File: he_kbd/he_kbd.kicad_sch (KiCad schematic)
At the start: 47 parts, among them U1 CD74HC4067M, U2 CD74HC4067M, U3 CD74HC4067M

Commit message: continue
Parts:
- U1, U2, U3: footprint Package_SO:TSSOP-24_4.4x7.8mm_P0.65mm -> Package_SO:SSOP-24_3.9x8.7mm_P0.635mm
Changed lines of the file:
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@@
 			)
 		)
-		(property "Footprint" "Package_SO:TSSOP-24_4.4x7.8mm_P0.65mm"
+		(property "Footprint" "Package_SO:SSOP-24_3.9x8.7mm_P0.635mm"
 			(at 130.81 59.69 0)
 			(effects
@@
 	)
 	(symbol
+		(lib_name "CD74HC4067M_1")
 		(lib_id "74xx:CD74HC4067M")
 		(at 63.5 120.65 270)
@@
 			)
 		)
-		(property "Footprint" "Package_SO:TSSOP-24_4.4x7.8mm_P0.65mm"
+		(property "Footprint" "Package_SO:SSOP-24_3.9x8.7mm_P0.635mm"
 			(at 38.1 143.51 0)
 			(effects
@@
 			)
 		)
-		(property "Footprint" "Package_SO:TSSOP-24_4.4x7.8mm_P0.65mm"
+		(property "Footprint" "Package_SO:SSOP-24_3.9x8.7mm_P0.635mm"
 			(at 215.9 59.69 0)
 			(effects

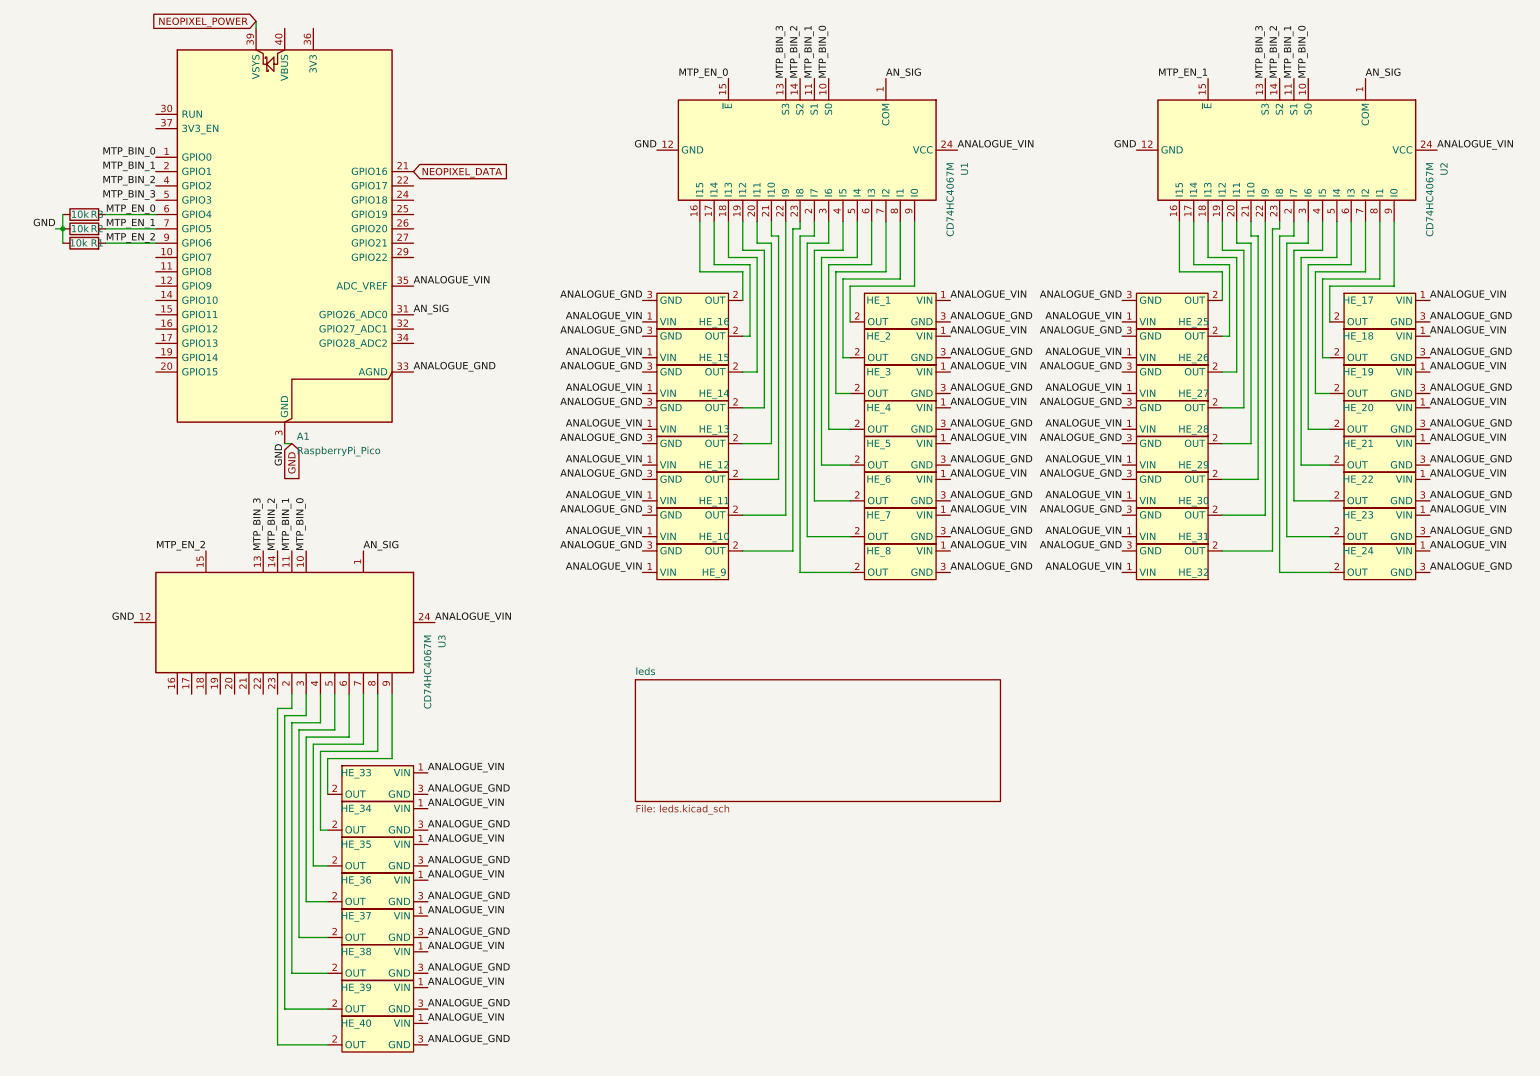
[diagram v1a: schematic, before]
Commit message: fixed up the net classes
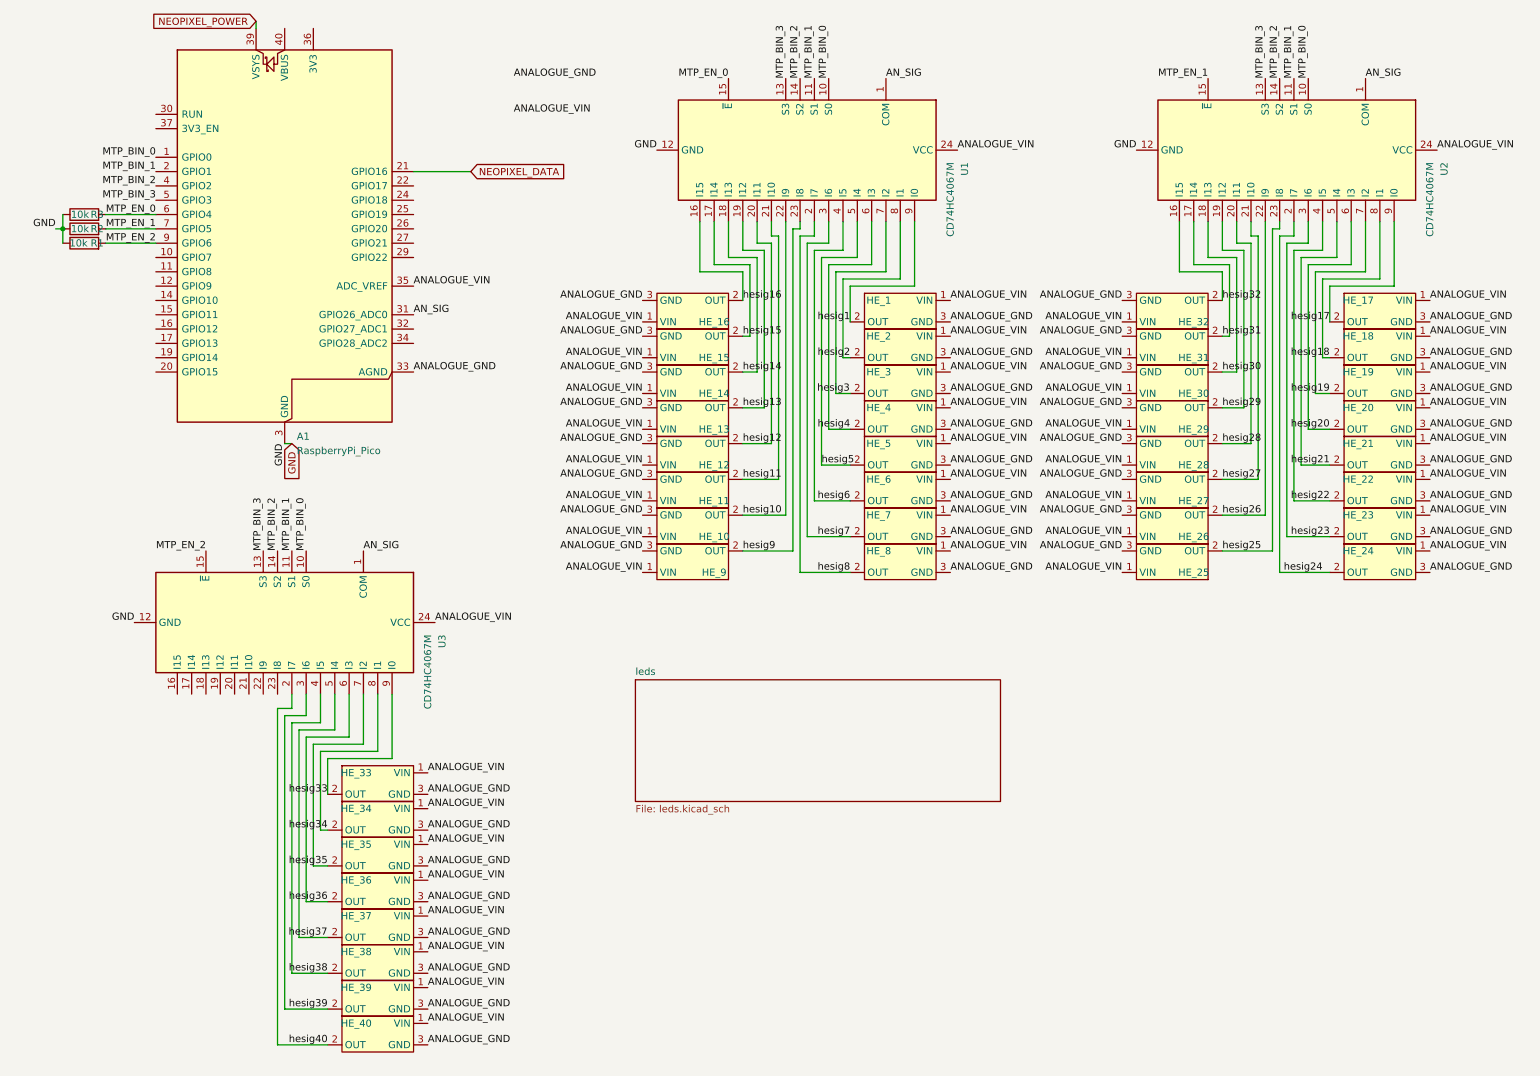
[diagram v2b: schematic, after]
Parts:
- U3: footprint Package_SO:SSOP-24_3.9x8.7mm_P0.635mm -> Package_SO:SOIC-24W_7.5x15.4mm_P1.27mm
- renumbered HE_32 to HE_25, HE_31 to HE_26, HE_30 to HE_27, HE_29 to HE_28, HE_28 to HE_29, HE_27 to HE_30, HE_26 to HE_31, HE_25 to HE_32
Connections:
- net hesig38: now reaches HE_38.2 (OUT), U3.4 (I5)
- net hesig31: now reaches HE_31.2 (OUT), U2.17 (I14)
- net hesig26: now reaches HE_26.2 (OUT), U2.22 (I9)
- net hesig2: now reaches HE_2.2 (OUT), U1.8 (I1)
- net hesig22: now reaches HE_22.2 (OUT), U2.4 (I5)
- net hesig12: now reaches HE_12.2 (OUT), U1.20 (I11)
- net hesig25: now reaches HE_25.2 (OUT), U2.23 (I8)
- net hesig34: now reaches HE_34.2 (OUT), U3.8 (I1)
- net hesig29: now reaches HE_29.2 (OUT), U2.19 (I12)
- net hesig7: now reaches HE_7.2 (OUT), U1.3 (I6)
- net hesig5: now reaches HE_5.2 (OUT), U1.5 (I4)
- net hesig13: now reaches HE_13.2 (OUT), U1.19 (I12)
- net hesig16: now reaches HE_16.2 (OUT), U1.16 (I15)
- net hesig15: now reaches HE_15.2 (OUT), U1.17 (I14)
- net hesig14: now reaches HE_14.2 (OUT), U1.18 (I13)
- net hesig8: now reaches HE_8.2 (OUT), U1.2 (I7)
- net hesig11: now reaches HE_11.2 (OUT), U1.21 (I10)
- net hesig10: now reaches HE_10.2 (OUT), U1.22 (I9)
- net hesig9: now reaches HE_9.2 (OUT), U1.23 (I8)
- net hesig6: now reaches HE_6.2 (OUT), U1.4 (I5)
- net hesig4: now reaches HE_4.2 (OUT), U1.6 (I3)
- net hesig3: now reaches HE_3.2 (OUT), U1.7 (I2)
- net hesig1: now reaches HE_1.2 (OUT), U1.9 (I0)
- net hesig19: now reaches HE_19.2 (OUT), U2.7 (I2)
- net hesig37: now reaches HE_37.2 (OUT), U3.5 (I4)
- net hesig36: now reaches HE_36.2 (OUT), U3.6 (I3)
- net hesig27: now reaches HE_27.2 (OUT), U2.21 (I10)
- net hesig17: now reaches HE_17.2 (OUT), U2.9 (I0)
- net hesig23: now reaches HE_23.2 (OUT), U2.3 (I6)
- net hesig40: now reaches HE_40.2 (OUT), U3.2 (I7)
- net hesig39: now reaches HE_39.2 (OUT), U3.3 (I6)
- net hesig35: now reaches HE_35.2 (OUT), U3.7 (I2)
- net hesig33: now reaches HE_33.2 (OUT), U3.9 (I0)
- net hesig32: now reaches HE_32.2 (OUT), U2.16 (I15)
- net hesig30: now reaches HE_30.2 (OUT), U2.18 (I13)
- net hesig24: now reaches HE_24.2 (OUT), U2.2 (I7)
- net hesig28: now reaches HE_28.2 (OUT), U2.20 (I11)
- net hesig21: now reaches HE_21.2 (OUT), U2.5 (I4)
- net hesig20: now reaches HE_20.2 (OUT), U2.6 (I3)
- net hesig18: now reaches HE_18.2 (OUT), U2.8 (I1)

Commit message: before updating pcb files, i added / changed some schematic components
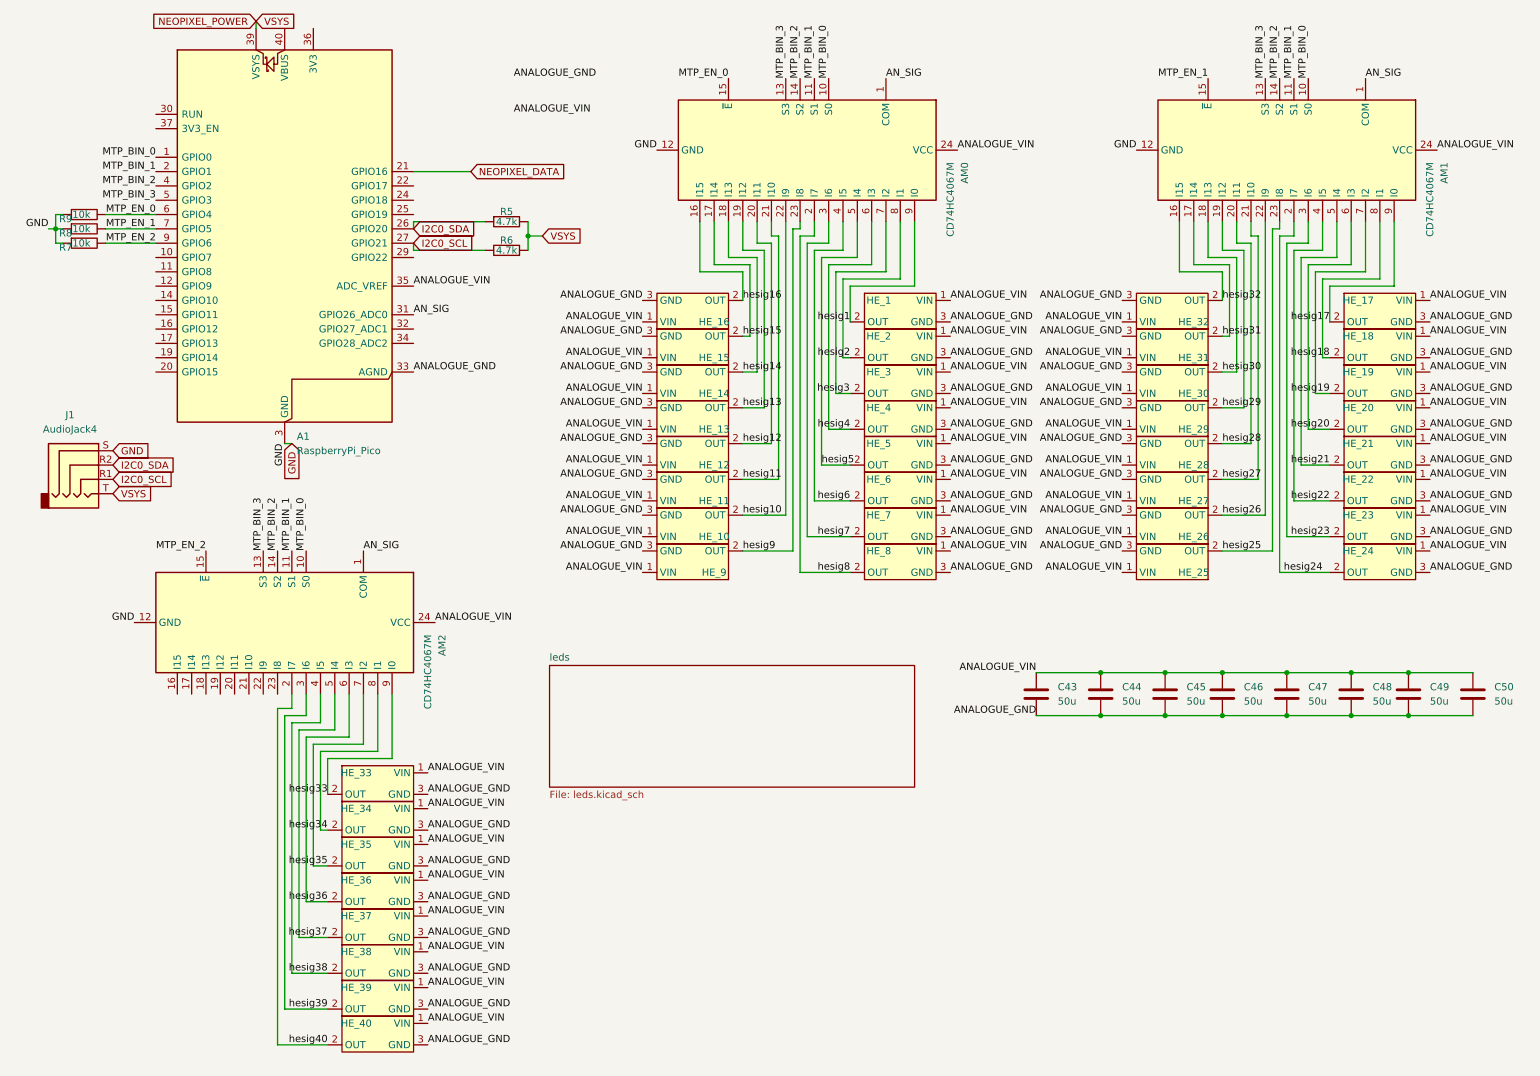
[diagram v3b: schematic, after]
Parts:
- removed R1, R2, R3: 10k, Resistor_SMD:R_0805_2012Metric, symbol Device:R
- added C43, C44, C45, C46, C47, C48, C49, C50: 50u, Inductor_SMD:L_0603_1608Metric, symbol PCM_Capacitor_US_AKL:C_0805
- added J1: AudioJack4, symbol Connector_Audio:AudioJack4
- added R5, R6: 4.7k, Resistor_SMD:R_0402_1005Metric, symbol PCM_SL_Resistors:4.7k
- added R7, R8, R9: 10k, Resistor_THT:R_Axial_DIN0207_L6.3mm_D2.5mm_P10.16mm_Horizontal, symbol PCM_SL_Resistors:10k
- AM0: renamed from U1; footprint Package_SO:SSOP-24_3.9x8.7mm_P0.635mm -> Package_SO:SSOP-24_5.3x8.2mm_P0.65mm
- AM1: renamed from U2; footprint Package_SO:SSOP-24_3.9x8.7mm_P0.635mm -> Package_SO:SSOP-24_5.3x8.2mm_P0.65mm
- AM2: renamed from U3; footprint Package_SO:SOIC-24W_7.5x15.4mm_P1.27mm -> Package_SO:SSOP-24_5.3x8.2mm_P0.65mm
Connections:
- net ANALOGUE_GND: now also C43.2, C44.2, C45.2, C46.2, C47.2, C48.2, C49.2, C50.2
- net ANALOGUE_VIN: now also C43.1, C44.1, C45.1, C46.1, C47.1, C48.1, C49.1, C50.1
- net GND: now also J1.S, R7.1, R8.1, R9.1
- net MTP_EN_0: now also R9.2
- net MTP_EN_1: now also R8.2
- net MTP_EN_2: now also R7.2
- net NEOPIXEL_POWER: now also J1.T, R5.2, R6.1
- net I2C0_SDA: now reaches A1.26 (GPIO20)
- net I2C0_SDA: now also J1.R2, R5.1
- net I2C0_SCL: now reaches A1.27 (GPIO21)
- net I2C0_SCL: now also J1.R1, R6.2

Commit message: much more organised now
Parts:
- R7, R8, R9: footprint Resistor_THT:R_Axial_DIN0207_L6.3mm_D2.5mm_P10.16mm_Horizontal -> Resistor_SMD:R_0603_1608Metric_Pad0.98x0.95mm_HandSolder
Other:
- added sheet Switch profiles (switches.kicad_sch)
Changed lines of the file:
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@@
 			)
 		)
-		(property "Footprint" "Resistor_THT:R_Axial_DIN0207_L6.3mm_D2.5mm_P10.16mm_Horizontal"
+		(property "Footprint" "Resistor_SMD:R_0603_1608Metric_Pad0.98x0.95mm_HandSolder"
 			(at 27.559 57.658 0)
 			(effects
@@
 			)
 		)
-		(property "Footprint" "Resistor_THT:R_Axial_DIN0207_L6.3mm_D2.5mm_P10.16mm_Horizontal"
+		(property "Footprint" "Resistor_SMD:R_0603_1608Metric_Pad0.98x0.95mm_HandSolder"
 			(at 27.559 52.578 0)
 			(effects
@@
 			)
 		)
-		(property "Footprint" "Resistor_THT:R_Axial_DIN0207_L6.3mm_D2.5mm_P10.16mm_Horizontal"
+		(property "Footprint" "Resistor_SMD:R_0603_1608Metric_Pad0.98x0.95mm_HandSolder"
 			(at 27.559 55.118 0)
 			(effects
@@
 				)
 			)
+		)
+	)
+	(sheet
+		(at 196.85 148.59)
+		(size 71.12 11.43)
+		(exclude_from_sim no)
+		(in_bom yes)
+		(on_board yes)
+		(dnp no)
+		(fields_autoplaced yes)
+		(stroke
+			(width 0.1524)
+			(type solid)
+		)
+		(fill
+			(color 0 0 0 0.0000)
+		)
+		(property "Sheetname" "Switch profiles"
+			(at 196.85 147.8784 0)
+			(effects
+				(font
+					(size 1.27 1.27)
+				)
+				(justify left bottom)
+			)
+		)
+		(property "Sheetfile" "switches.kicad_sch"
+			(at 196.85 160.6046 0)
+			(effects
+				(font
+					(size 1.27 1.27)
+				)
+				(justify left top)
+			)
+		)
+		(instances
+			(project "he_kbd"
+				(path "/ec6e5a97-af17-41bd-90dd-eb7235b0e08a"
+					(page "3")
+				)
+			)

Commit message: more progress
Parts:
- removed HE_36, HE_37, HE_38, HE_39, HE_40: ~, Package_TO_SOT_SMD:SOT-23-3, symbol he_lib:GH39FKSW
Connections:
- net hesig36: no longer names the net of AM2.6 (I3)
- net hesig37: no longer names the net of AM2.5 (I4)
- net hesig38: no longer names the net of AM2.4 (I5)
- net hesig39: no longer names the net of AM2.3 (I6)
- net hesig40: no longer names the net of AM2.2 (I7)

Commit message: realised have to change capacitor footprint entirely
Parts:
- C43, C44, C45, C46, C47, C48, C49, C50: footprint Inductor_SMD:L_0603_1608Metric -> PCM_Capacitor_SMD_AKL:C_0805_2012Metric_Pad1.18x1.45mm_HandSolder
- R5, R6: footprint Resistor_SMD:R_0402_1005Metric -> Resistor_SMD:R_0805_2012Metric_Pad1.20x1.40mm_HandSolder
- R7, R8, R9: footprint Resistor_SMD:R_0603_1608Metric_Pad0.98x0.95mm_HandSolder -> Resistor_SMD:R_0805_2012Metric_Pad1.20x1.40mm_HandSolder
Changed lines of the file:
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@@
 			)
 		)
-		(property "Footprint" "Inductor_SMD:L_0603_1608Metric"
+		(property "Footprint" "PCM_Capacitor_SMD_AKL:C_0805_2012Metric_Pad1.18x1.45mm_HandSolder"
 			(at 219.4052 137.16 0)
 			(effects
@@
 			)
 		)
-		(property "Footprint" "Resistor_SMD:R_0402_1005Metric"
+		(property "Footprint" "Resistor_SMD:R_0805_2012Metric_Pad1.20x1.40mm_HandSolder"
 			(at 102.489 53.848 0)
 			(effects
@@
 			)
 		)
-		(property "Footprint" "Resistor_SMD:R_0603_1608Metric_Pad0.98x0.95mm_HandSolder"
+		(property "Footprint" "Resistor_SMD:R_0805_2012Metric_Pad1.20x1.40mm_HandSolder"
 			(at 27.559 57.658 0)
 			(effects
@@
 			)
 		)
-		(property "Footprint" "Resistor_SMD:R_0402_1005Metric"
+		(property "Footprint" "Resistor_SMD:R_0805_2012Metric_Pad1.20x1.40mm_HandSolder"
 			(at 100.711 50.292 0)
 			(effects
@@
 			)
 		)
-		(property "Footprint" "Inductor_SMD:L_0603_1608Metric"
+		(property "Footprint" "PCM_Capacitor_SMD_AKL:C_0805_2012Metric_Pad1.18x1.45mm_HandSolder"
 			(at 229.5652 137.16 0)
 			(effects
@@
 			)
 		)
-		(property "Footprint" "Inductor_SMD:L_0603_1608Metric"
+		(property "Footprint" "PCM_Capacitor_SMD_AKL:C_0805_2012Metric_Pad1.18x1.45mm_HandSolder"
 			(at 252.4252 137.16 0)
 			(effects
@@
 			)
 		)
-		(property "Footprint" "Resistor_SMD:R_0603_1608Metric_Pad0.98x0.95mm_HandSolder"
+		(property "Footprint" "Resistor_SMD:R_0805_2012Metric_Pad1.20x1.40mm_HandSolder"
 			(at 27.559 52.578 0)
 			(effects
@@
 			)
 		)
-		(property "Footprint" "Inductor_SMD:L_0603_1608Metric"
+		(property "Footprint" "PCM_Capacitor_SMD_AKL:C_0805_2012Metric_Pad1.18x1.45mm_HandSolder"
 			(at 207.9752 137.16 0)
 			(effects
@@
 			)
 		)
-		(property "Footprint" "Inductor_SMD:L_0603_1608Metric"
+		(property "Footprint" "PCM_Capacitor_SMD_AKL:C_0805_2012Metric_Pad1.18x1.45mm_HandSolder"
 			(at 196.5452 137.16 0)
 			(effects
@@
 			)
 		)
-		(property "Footprint" "Resistor_SMD:R_0603_1608Metric_Pad0.98x0.95mm_HandSolder"
+		(property "Footprint" "Resistor_SMD:R_0805_2012Metric_Pad1.20x1.40mm_HandSolder"
 			(at 27.559 55.118 0)
 			(effects
@@
 			)
 		)
-		(property "Footprint" "Inductor_SMD:L_0603_1608Metric"
+		(property "Footprint" "PCM_Capacitor_SMD_AKL:C_0805_2012Metric_Pad1.18x1.45mm_HandSolder"
 			(at 274.0152 137.16 0)
 			(effects
@@
 			)
 		)
-		(property "Footprint" "Inductor_SMD:L_0603_1608Metric"
+		(property "Footprint" "PCM_Capacitor_SMD_AKL:C_0805_2012Metric_Pad1.18x1.45mm_HandSolder"
 			(at 262.5852 137.16 0)
 			(effects
@@
 			)
 		)
-		(property "Footprint" "Inductor_SMD:L_0603_1608Metric"
+		(property "Footprint" "PCM_Capacitor_SMD_AKL:C_0805_2012Metric_Pad1.18x1.45mm_HandSolder"
 			(at 240.9952 137.16 0)
 			(effects
